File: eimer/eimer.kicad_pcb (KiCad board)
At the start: 2 copper layers, 72 x 72 mm, 71 parts, among them J3 Conn_01x03, J4 USB_C_Receptacle_USB2.0_14P, SW1 SW_Push, SW2 SW_Push, U1 RP2040, U2 MCP1700x-330xxTT, U3 TPS61221DCK, U4 W25Q16JVUXIQ TR, U5 LIS2DW12, Y1 12 MHz

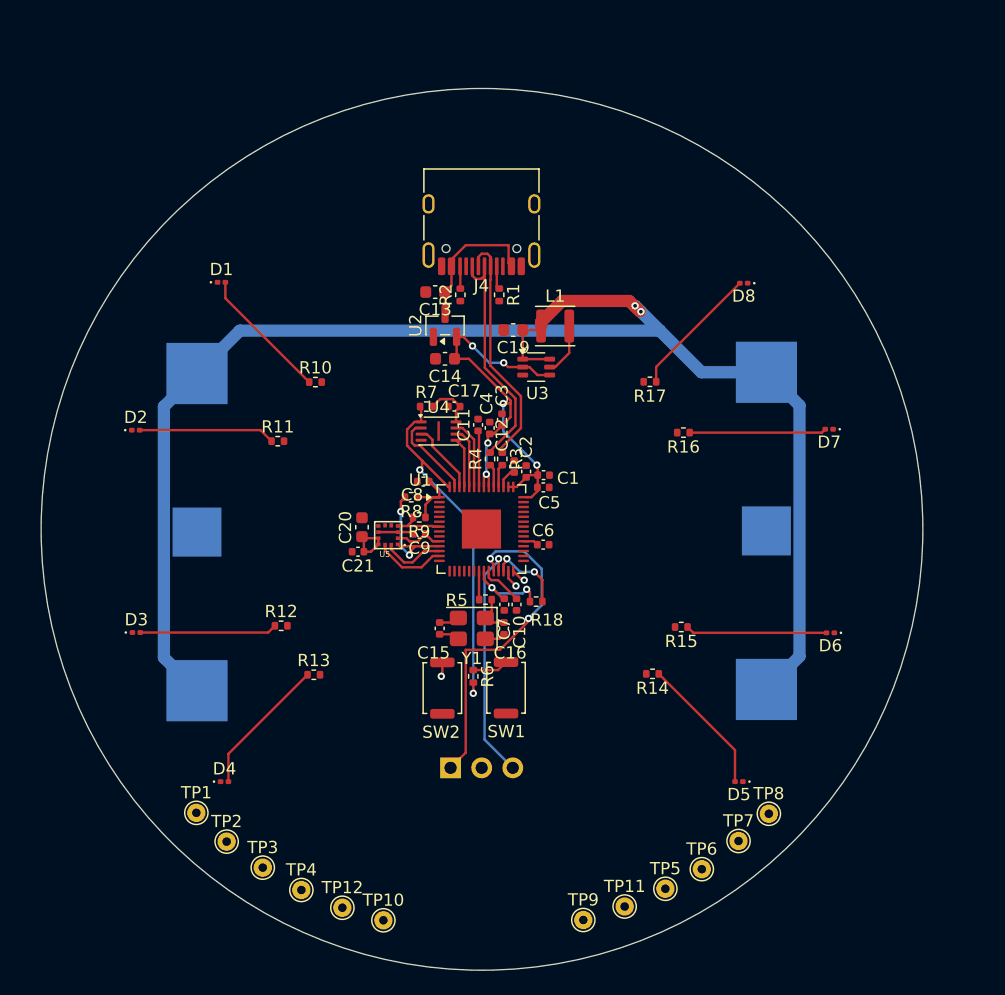
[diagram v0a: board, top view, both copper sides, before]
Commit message: routing leds
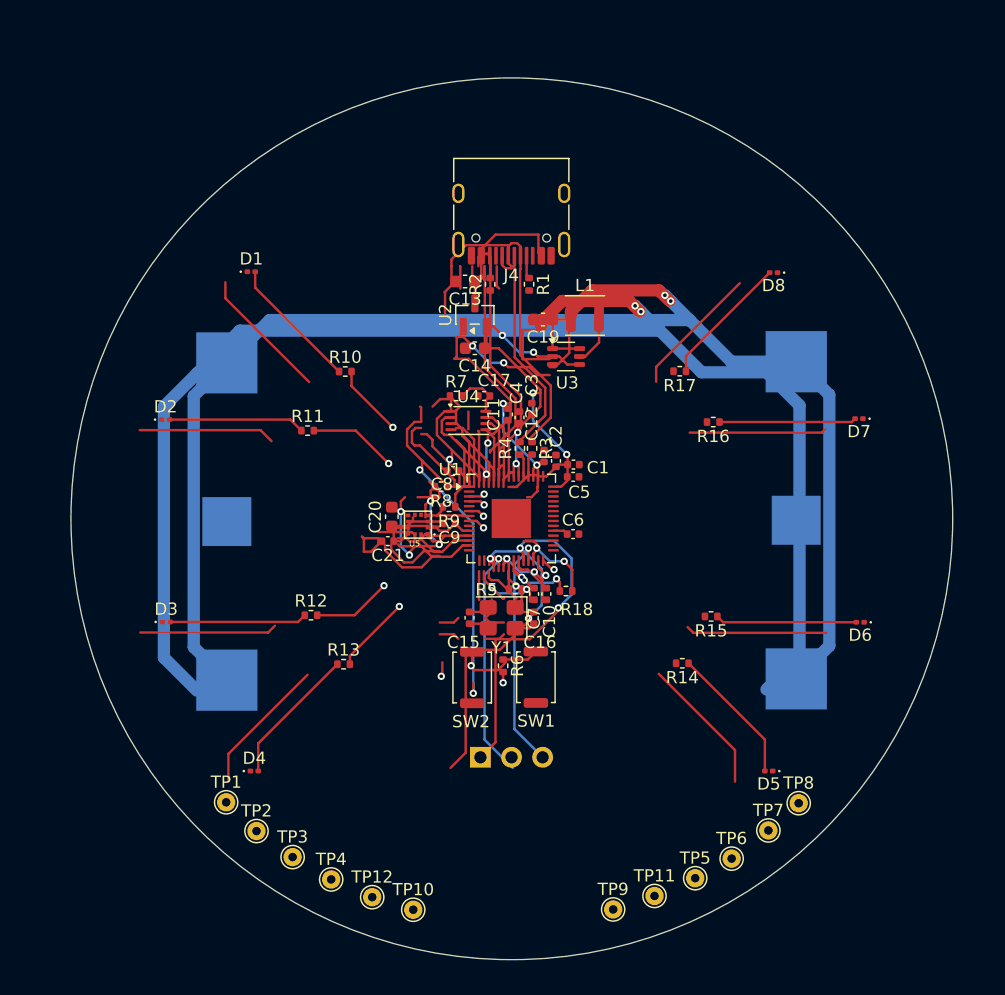
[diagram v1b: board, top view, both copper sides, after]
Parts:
- moved C12 2.58 mm to (77.2, 88.3)
- moved C15 2.58 mm to (71.1, 101.5)
- moved C16 2.58 mm to (76.4, 101.5)
- moved C3 2.58 mm to (76.2, 84.4)
- moved C4 2.58 mm to (75.2, 85.1)
- moved C5 2.58 mm to (79.6, 90.0)
- moved C8 2.58 mm to (69.8, 89.5)
- moved C9 2.58 mm to (69.5, 93.8)
- moved D5 2.58 mm to (95.6, 114.0)
- moved D6 2.58 mm to (103.0, 101.8)
- moved J3 2.58 mm to (72.0, 112.9)
- moved J4 2.58 mm to (74.5, 67.9)
- moved R15 2.58 mm to (90.9, 101.4)
- moved R16 2.58 mm to (91.0, 85.5)
- moved R17 2.58 mm to (88.3, 81.3)
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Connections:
- R10 pad 2: GPIO11 -> GPIO1
- R11 pad 2: GPIO12 -> GPIO2
- R12 pad 2: GPIO13 -> GPIO4
- R13 pad 2: unconnected-(R13-Pad2) -> GPIO6
- R14 pad 2: GPIO15 -> GPIO26/ADC0
- R15 pad 2: GPIO16 -> GPIO27/ADC1
- R16 pad 2: GPIO17 -> GPIO28/ADC2
- R17 pad 2: GPIO18 -> GPIO29/ADC3
- TP1 pad 1: GPIO26/ADC0 -> unconnected-(TP1-Pad1)
- TP2 pad 1: GPIO27/ADC1 -> unconnected-(TP2-Pad1)
- TP3 pad 1: GPIO28/ADC2 -> unconnected-(TP3-Pad1)
- TP4 pad 1: GPIO29/ADC3 -> unconnected-(TP4-Pad1)
- TP5 pad 1: GPIO20 -> unconnected-(TP5-Pad1)
- TP6 pad 1: GPIO22 -> unconnected-(TP6-Pad1)
- TP7 pad 1: GPIO23 -> unconnected-(TP7-Pad1)
- TP8 pad 1: GPIO24 -> unconnected-(TP8-Pad1)
- U1 pad 14: GPIO11 -> unconnected-(U1-GPIO11-Pad14)
- U1 pad 15: GPIO12 -> unconnected-(U1-GPIO12-Pad15)
- U1 pad 16: GPIO13 -> unconnected-(U1-GPIO13-Pad16)
- U1 pad 17: GPIO14 -> unconnected-(U1-GPIO14-Pad17)
- U1 pad 18: GPIO15 -> unconnected-(U1-GPIO15-Pad18)
- U1 pad 27: GPIO16 -> unconnected-(U1-GPIO16-Pad27)
- U1 pad 28: GPIO17 -> unconnected-(U1-GPIO17-Pad28)
- U1 pad 29: GPIO18 -> unconnected-(U1-GPIO18-Pad29)
- U1 pad 3: unconnected-(U1-GPIO1-Pad3) -> GPIO1
- U1 pad 31: GPIO20 -> unconnected-(U1-GPIO20-Pad31)
- U1 pad 34: GPIO22 -> unconnected-(U1-GPIO22-Pad34)
- U1 pad 35: GPIO23 -> unconnected-(U1-GPIO23-Pad35)
- U1 pad 36: GPIO24 -> unconnected-(U1-GPIO24-Pad36)
- U1 pad 4: unconnected-(U1-GPIO2-Pad4) -> GPIO2
- U1 pad 6: unconnected-(U1-GPIO4-Pad6) -> GPIO4
- U1 pad 8: unconnected-(U1-GPIO6-Pad8) -> GPIO6
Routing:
- net Net-(BT1-+): track 124.2 -> 248.4 mm, vias 2 -> 4
- net +3.3V: track 65.9 -> 130.5 mm, vias 8 -> 16
- net SWCLK: track 27.2 -> 54.5 mm, vias 2 -> 4
- net USB_D+: track 19.9 -> 39.8 mm
- net USB_D-: track 19.8 -> 39.7 mm
- net SWDIO: track 19.5 -> 39.0 mm, vias 1 -> 2
- net VBUS: track 11.7 -> 23.3 mm
- net Net-(D6-A): track 11.5 -> 23.1 mm
- net Net-(D4-A): track 11.4 -> 22.8 mm
- net Net-(D5-A): track 11.4 -> 22.8 mm
- net Net-(D3-A): track 11.2 -> 22.4 mm
- net Net-(D7-A): track 11.2 -> 22.4 mm
- net Net-(D2-A): track 11.1 -> 22.3 mm
- net Net-(D1-A): track 11.0 -> 22.0 mm
- net Net-(D8-A): track 10.9 -> 21.8 mm
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
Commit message: revert
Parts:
- moved J4 4.40 mm to (73.8, 63.5)
- moved C20 4.40 mm to (64.1, 88.9)
- moved C8 4.40 mm to (69.1, 85.1)
- moved C9 4.40 mm to (68.8, 89.4)
- moved D6 4.40 mm to (102.3, 97.5)
- moved R17 4.40 mm to (87.6, 77.0)
- moved R7 4.40 mm to (69.3, 79.0)
- moved TP10 4.40 mm to (65.8, 121.0)
- moved TP11 4.40 mm to (85.5, 119.8)
- moved TP6 4.40 mm to (91.8, 116.8)
- moved TP7 4.40 mm to (94.8, 114.5)
- moved TP9 4.40 mm to (82.1, 121.0)
- moved U1 4.40 mm to (73.8, 89.0)
- moved U4 4.40 mm to (70.3, 81.0)
- moved C21 4.40 mm to (63.7, 90.9)
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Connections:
- R10 pad 2: GPIO1 -> GPIO11
- R11 pad 2: GPIO2 -> GPIO12
- R12 pad 2: GPIO4 -> GPIO13
- R13 pad 2: GPIO6 -> unconnected-(R13-Pad2)
- R14 pad 2: GPIO26/ADC0 -> GPIO15
- R15 pad 2: GPIO27/ADC1 -> GPIO16
- R16 pad 2: GPIO28/ADC2 -> GPIO17
- R17 pad 2: GPIO29/ADC3 -> GPIO18
- TP1 pad 1: unconnected-(TP1-Pad1) -> GPIO26/ADC0
- TP2 pad 1: unconnected-(TP2-Pad1) -> GPIO27/ADC1
- TP3 pad 1: unconnected-(TP3-Pad1) -> GPIO28/ADC2
- TP4 pad 1: unconnected-(TP4-Pad1) -> GPIO29/ADC3
- TP5 pad 1: unconnected-(TP5-Pad1) -> GPIO20
- TP6 pad 1: unconnected-(TP6-Pad1) -> GPIO22
- TP7 pad 1: unconnected-(TP7-Pad1) -> GPIO23
- TP8 pad 1: unconnected-(TP8-Pad1) -> GPIO24
- U1 pad 14: unconnected-(U1-GPIO11-Pad14) -> GPIO11
- U1 pad 15: unconnected-(U1-GPIO12-Pad15) -> GPIO12
- U1 pad 16: unconnected-(U1-GPIO13-Pad16) -> GPIO13
- U1 pad 17: unconnected-(U1-GPIO14-Pad17) -> GPIO14
- U1 pad 18: unconnected-(U1-GPIO15-Pad18) -> GPIO15
- U1 pad 27: unconnected-(U1-GPIO16-Pad27) -> GPIO16
- U1 pad 28: unconnected-(U1-GPIO17-Pad28) -> GPIO17
- U1 pad 29: unconnected-(U1-GPIO18-Pad29) -> GPIO18
- U1 pad 3: GPIO1 -> unconnected-(U1-GPIO1-Pad3)
- U1 pad 31: unconnected-(U1-GPIO20-Pad31) -> GPIO20
- U1 pad 34: unconnected-(U1-GPIO22-Pad34) -> GPIO22
- U1 pad 35: unconnected-(U1-GPIO23-Pad35) -> GPIO23
- U1 pad 36: unconnected-(U1-GPIO24-Pad36) -> GPIO24
- U1 pad 4: GPIO2 -> unconnected-(U1-GPIO2-Pad4)
- U1 pad 6: GPIO4 -> unconnected-(U1-GPIO4-Pad6)
- U1 pad 8: GPIO6 -> unconnected-(U1-GPIO6-Pad8)
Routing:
- net Net-(BT1-+): track 248.4 -> 124.2 mm, vias 4 -> 2
- net +3.3V: track 130.5 -> 65.9 mm, vias 16 -> 8
- net SWCLK: track 54.5 -> 27.2 mm, vias 4 -> 2
- net USB_D+: track 39.8 -> 19.9 mm
- net USB_D-: track 39.7 -> 19.8 mm
- net SWDIO: track 39.0 -> 19.5 mm, vias 2 -> 1
- net VBUS: track 23.3 -> 11.7 mm
- net Net-(D6-A): track 23.1 -> 11.5 mm
- net Net-(D4-A): track 22.8 -> 11.4 mm
- net Net-(D5-A): track 22.8 -> 11.4 mm
- net Net-(D3-A): track 22.4 -> 11.2 mm
- net Net-(D7-A): track 22.4 -> 11.2 mm
- net Net-(D2-A): track 22.3 -> 11.1 mm
- net Net-(D1-A): track 22.0 -> 11.0 mm
- net Net-(D8-A): track 21.8 -> 10.9 mm
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
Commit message: routed left leds again
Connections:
- R10 pad 2: GPIO11 -> GPIO1
- R11 pad 2: GPIO12 -> GPIO2
- R12 pad 2: GPIO13 -> GPIO4
- R13 pad 2: unconnected-(R13-Pad2) -> GPIO6
- R14 pad 2: GPIO15 -> GPIO26/ADC0
- R15 pad 2: GPIO16 -> GPIO27/ADC1
- R16 pad 2: GPIO17 -> GPIO28/ADC2
- R17 pad 2: GPIO18 -> GPIO29/ADC3
- TP1 pad 1: GPIO26/ADC0 -> unconnected-(TP1-Pad1)
- TP2 pad 1: GPIO27/ADC1 -> unconnected-(TP2-Pad1)
- TP3 pad 1: GPIO28/ADC2 -> unconnected-(TP3-Pad1)
- TP4 pad 1: GPIO29/ADC3 -> unconnected-(TP4-Pad1)
- TP5 pad 1: GPIO20 -> unconnected-(TP5-Pad1)
- TP6 pad 1: GPIO22 -> unconnected-(TP6-Pad1)
- TP7 pad 1: GPIO23 -> unconnected-(TP7-Pad1)
- TP8 pad 1: GPIO24 -> unconnected-(TP8-Pad1)
- U1 pad 14: GPIO11 -> unconnected-(U1-GPIO11-Pad14)
- U1 pad 15: GPIO12 -> unconnected-(U1-GPIO12-Pad15)
- U1 pad 16: GPIO13 -> unconnected-(U1-GPIO13-Pad16)
- U1 pad 17: GPIO14 -> unconnected-(U1-GPIO14-Pad17)
- U1 pad 18: GPIO15 -> unconnected-(U1-GPIO15-Pad18)
- U1 pad 27: GPIO16 -> unconnected-(U1-GPIO16-Pad27)
- U1 pad 28: GPIO17 -> unconnected-(U1-GPIO17-Pad28)
- U1 pad 29: GPIO18 -> unconnected-(U1-GPIO18-Pad29)
- U1 pad 3: unconnected-(U1-GPIO1-Pad3) -> GPIO1
- U1 pad 31: GPIO20 -> unconnected-(U1-GPIO20-Pad31)
- U1 pad 34: GPIO22 -> unconnected-(U1-GPIO22-Pad34)
- U1 pad 35: GPIO23 -> unconnected-(U1-GPIO23-Pad35)
- U1 pad 36: GPIO24 -> unconnected-(U1-GPIO24-Pad36)
- U1 pad 4: unconnected-(U1-GPIO2-Pad4) -> GPIO2
- U1 pad 6: unconnected-(U1-GPIO4-Pad6) -> GPIO4
- U1 pad 8: unconnected-(U1-GPIO6-Pad8) -> GPIO6
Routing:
- net QSPI_SS: track 30.6 -> 10.6 mm
- net GPIO6: track 0.00 -> 18.6 mm, vias 0 -> 2
- net GPIO4: track 0.00 -> 18.5 mm, vias 0 -> 2
- net GPIO2: track 0.00 -> 18.0 mm, vias 0 -> 2
- net GPIO1: track 0.00 -> 17.3 mm, vias 0 -> 2
- net unconnected-(U1-GPIO16-Pad27): track 0.00 -> 1.47 mm, vias 0 -> 1
- net GPIO16: track 1.47 -> 0.00 mm, vias 1 -> 0
- net unconnected-(U1-GPIO17-Pad28): track 0.00 -> 1.20 mm, vias 0 -> 1
- net GPIO17: track 1.20 -> 0.00 mm, vias 1 -> 0

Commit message: routed all left side gpios
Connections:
- TP1 pad 1: unconnected-(TP1-Pad1) -> GPIO11
- TP2 pad 1: unconnected-(TP2-Pad1) -> GPIO12
- TP3 pad 1: unconnected-(TP3-Pad1) -> GPIO13
- TP4 pad 1: unconnected-(TP4-Pad1) -> GPIO15
- U1 pad 14: unconnected-(U1-GPIO11-Pad14) -> GPIO11
- U1 pad 15: unconnected-(U1-GPIO12-Pad15) -> GPIO12
- U1 pad 16: unconnected-(U1-GPIO13-Pad16) -> GPIO13
- U1 pad 18: unconnected-(U1-GPIO15-Pad18) -> GPIO15
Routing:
- net GPIO15: track 0.00 -> 31.5 mm
- net GPIO13: track 0.00 -> 30.7 mm
- net GPIO12: track 0.00 -> 29.6 mm
- net GPIO11: track 0.00 -> 29.4 mm
